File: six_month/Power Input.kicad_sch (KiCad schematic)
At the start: 4 parts, among them U1 GT-USB-7010ASV

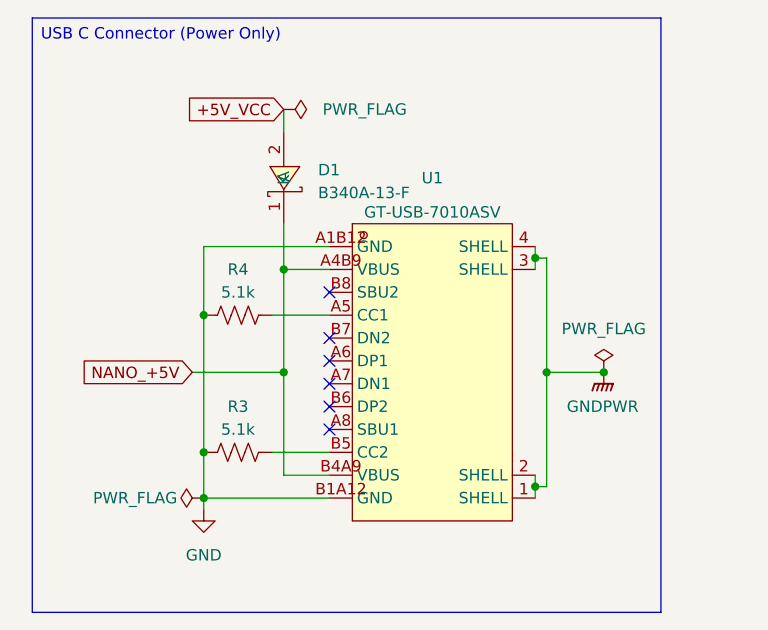
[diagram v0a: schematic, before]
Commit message: Changes
Removed the microphone idea, added a DAC for Bluetooth to Line out. Allows for external speakers to be connected via an Aux cable
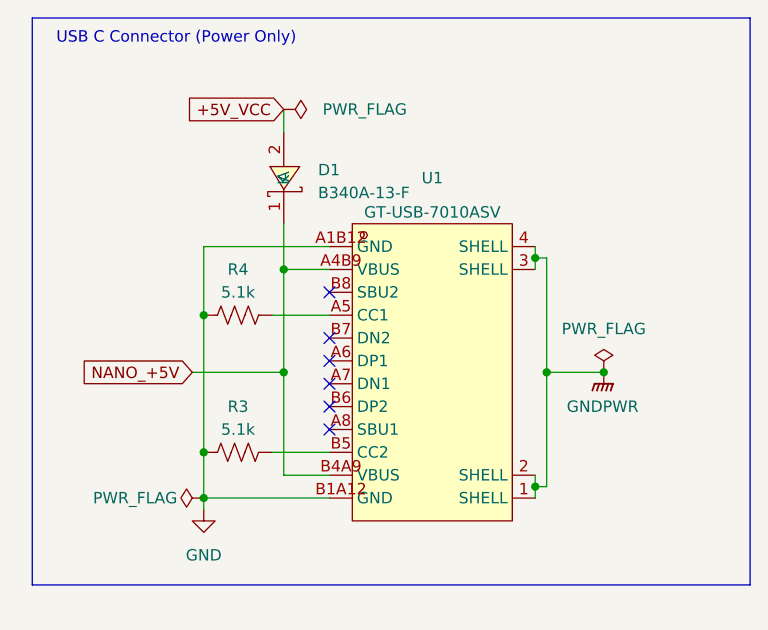
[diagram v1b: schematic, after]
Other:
- note added: "USB C Connector (Power Only)"
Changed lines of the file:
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@@
 	(generator_version "9.0")
 	(paper "A5")
-	(text_box "USB C Connector (Power Only)"
-		(exclude_from_sim no)
-		(at 12.7 12.7 0)
-		(size 69.85 66.04)
-		(margins 0.9525 0.9525 0.9525 0.9525)
+	(rectangle
+		(start 12.7 12.7)
+		(end 92.456 75.692)
 		(stroke
 			(width 0)
-			(type solid)
+			(type default)
 		)
 		(fill
 			(type none)
 		)
+	)
+	(text "USB C Connector (Power Only)"
+		(exclude_from_sim no)
+		(at 28.702 14.986 0)
 		(effects
 			(font
 				(size 1.27 1.27)
 			)
-			(justify left top)
 		)
 	)
